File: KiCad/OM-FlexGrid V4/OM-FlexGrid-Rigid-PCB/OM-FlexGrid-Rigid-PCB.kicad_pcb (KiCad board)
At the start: 4 copper layers, 65.5 x 33 mm, 56 parts, among them IC1 ICM-42688-P, J1 Conn_01x06_Pin, J2 BAT Terminal, J3 Conn_01x20, J4 USB_C_Receptacle, J5 Conn_01x02, J6 Conn_01x03_Pin, J7 Conn_01x02_Pin, Q1 IRLML2060, Q2 VP0610T or BSS84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

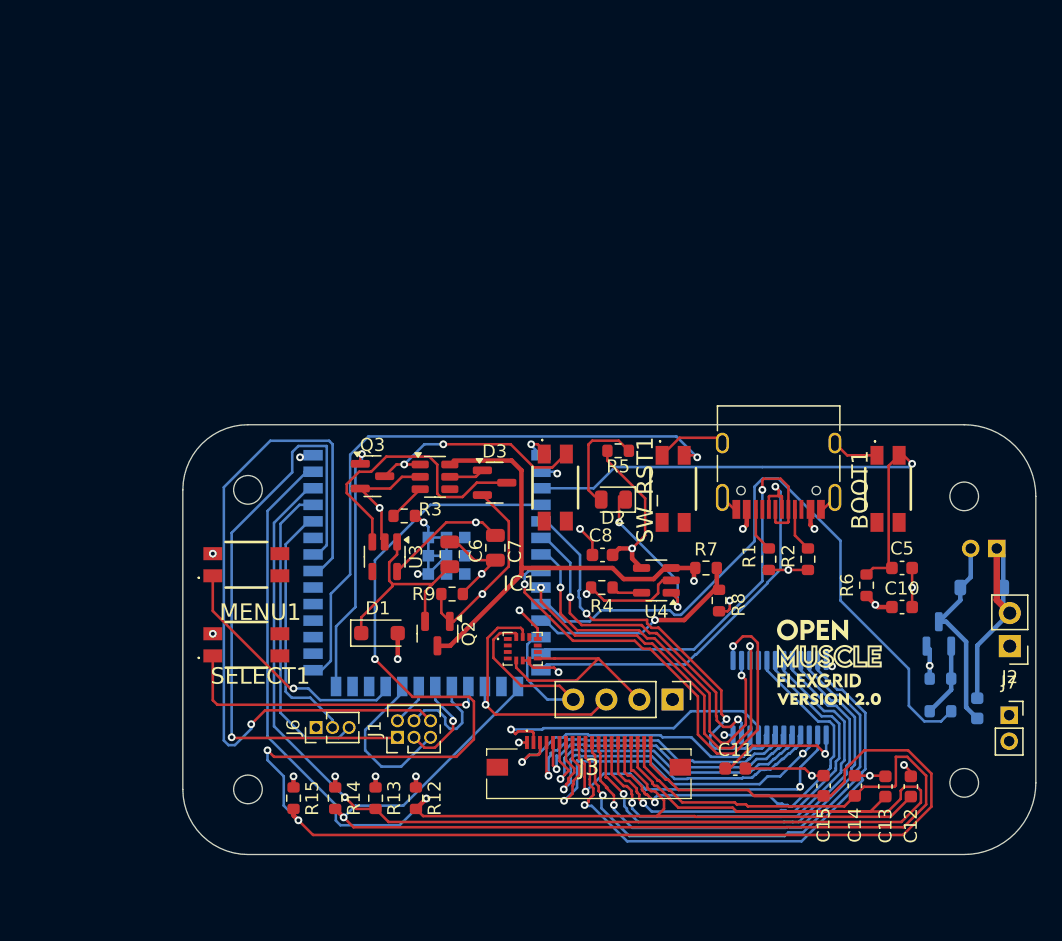
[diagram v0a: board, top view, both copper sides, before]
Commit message: V4 progress: SD card reader, RGB status LED, slimmer reoriented layout
What landed in V4 (Rigid PCB):
- microSD card socket added (data logging / model storage on-device)
- Discrete RGB status LED (5050 common-cathode driven by 3 PWM GPIOs,
  zero quiescent current vs WS2812 family; status palette ready to
  drive from firmware)
- Board orientation flipped for a slimmer profile that hugs the
  bracelet better; component placement reworked to clear the new
  long axis

Production artifacts included:
- V4 schematic (24K lines, full reroute from V3 baseline)
- V4 PCB with new placement
- V4 Gerber zip (OM-FlexGrid-Rigid-V4-Gerber.zip)
- JLCPCB plugin output dir (BOM + CPL ready for upload)
- Pick-and-place position file (.pos)
- 3D STEP export for mechanical fit check
- Per-revision backup snapshots from the design session

Housekeeping:
- .gitignore extended for KiCad transients (_autosave-*, *.lck,
  ~*.lck, tmp*.rpt) and .claude/ session metadata
- V3 working tree edits are intentionally left untouched; they
  belong to the V3 production-finalization branch of work

Status: V4 is "almost done" per the design pass; not yet ordered
or fab-validated. Treat this commit as a checkpoint, not a release.
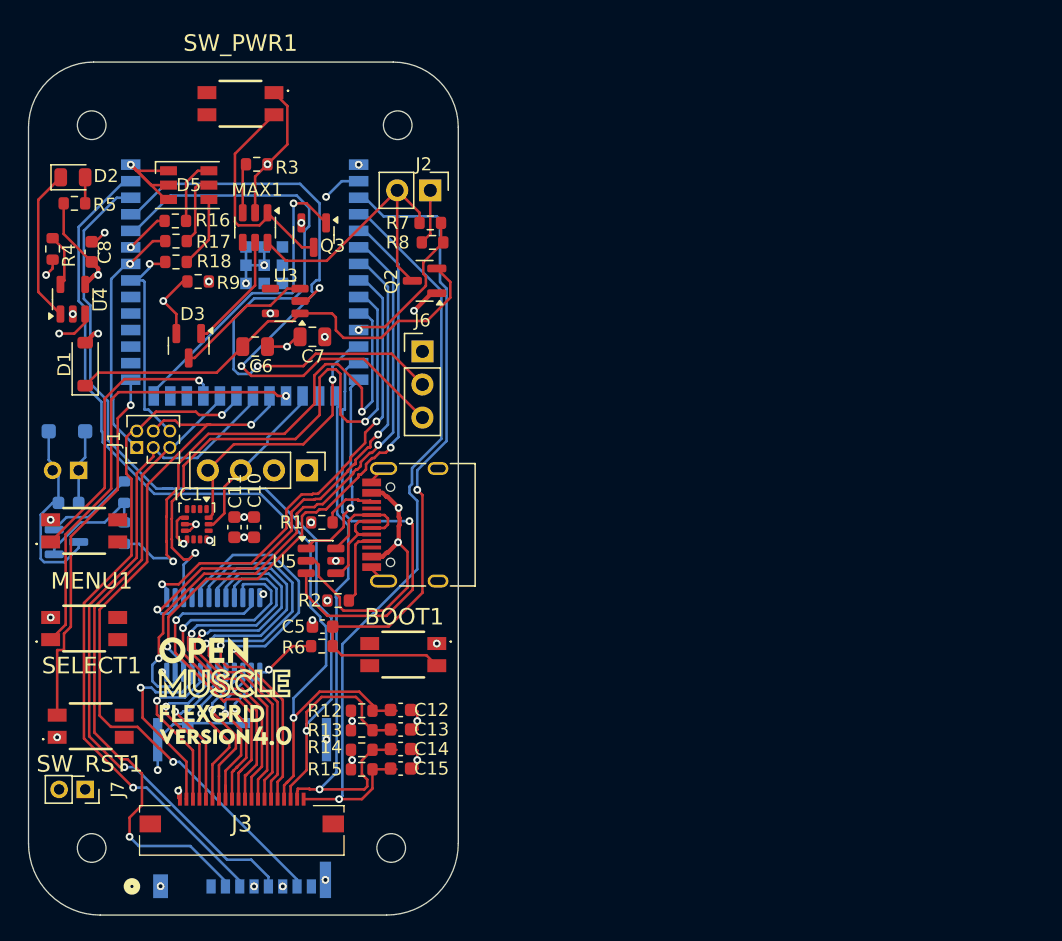
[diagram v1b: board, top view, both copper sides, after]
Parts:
- added D5: LED_RGB, LED_SMD:LED_RGB_PLCC-6, F.Cu at (152.4, 80.1)
- added J9: Micro_SD_Card, footprints:CONN_503398-1892_MOL, B.Cu at (156.6, 128.3)
- added R16: 330, Resistor_SMD:R_0603_1608Metric, F.Cu at (151.4, 82.8)
- added R17: 330, Resistor_SMD:R_0603_1608Metric, F.Cu at (151.5, 84.4)
- added R18: 330, Resistor_SMD:R_0603_1608Metric, F.Cu at (151.5, 86.0)
- added U5: USBLC6-2SC6, Package_TO_SOT_SMD:SOT-23-6, F.Cu at (162.6, 109.0)
- D1: footprint Diode_SMD:D_SOD-123F -> Diode_SMD:D_SOD-123
- D4: footprint Diode_SMD:D_SOD-123 -> Diode_SMD:D_SOD-123F
- IC1: footprint ICM-42688-P:IIM42352 -> Package_LGA:LGA-14_3x2.5mm_P0.5mm_LayoutBorder3x4y
- J6: footprint Connector_PinHeader_1.27mm:PinHeader_1x03_P1.27mm_Vertical -> Connector_PinHeader_2.54mm:PinHeader_1x03_P2.54mm_Vertical
- moved C9 71.5 mm to (143.2, 104.5), turned to 0 degrees
- moved D4 71.3 mm to (143.1, 99.0)
- moved J7 71.2 mm to (144.5, 126.5), turned to -90 degrees
- moved J5 70.8 mm to (144.0, 102.0)
- moved Q1 67.4 mm to (143.1, 107.5), turned to 0 degrees
- moved H3 67.2 mm to (145.0, 131.0), turned to -90 degrees
- moved R11 64.3 mm to (147.5, 103.7), turned to -90 degrees
- moved R10 64.1 mm to (147.5, 106.8), turned to -90 degrees
- moved J2 56.6 mm to (171.0, 80.5), turned to -90 degrees
- moved H4 52.4 mm to (145.0, 75.5), turned to -90 degrees
- moved H2 51.6 mm to (168.0, 131.0), turned to -90 degrees
- moved C10 50.1 mm to (157.5, 106.4), turned to 90 degrees
- moved U4 49.7 mm to (143.6, 88.9), turned to 90 degrees
- moved R4 49.5 mm to (142.0, 85.0), turned to -90 degrees
- moved D2 48.3 mm to (143.6, 79.5), turned to 0 degrees
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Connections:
- J4 pad A6: D+ -> Net-(J4-D+-PadA6)
- J4 pad A7: D- -> Net-(J4-D--PadA7)
- J4 pad B6: D+ -> Net-(J4-D+-PadA6)
- J4 pad B7: D- -> Net-(J4-D--PadA7)
- U2 pad 35: unconnected-(U2-IO42-Pad35) -> GP42
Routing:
- net ROW_3: track 142.8 -> 60.5 mm, vias 3 -> 1
- net ROW_2: track 94.9 -> 43.2 mm
- net SPI_MISO: track 8.23 -> 57.7 mm, vias 0 -> 2
- net SPI_MOSI: track 3.31 -> 52.0 mm, vias 0 -> 2
- net SPI_SCK: track 7.78 -> 53.4 mm
- net GP40: track 57.7 -> 17.0 mm
- net ROW_1: track 112.3 -> 74.3 mm
- net CS: track 12.5 -> 49.3 mm, vias 0 -> 1
- net RX: track 19.2 -> 48.8 mm, vias 0 -> 1
- net GP41: track 48.4 -> 19.2 mm
- net +3V3: track 41.1 -> 12.8 mm, vias 5 -> 8
- net TX: track 24.0 -> 48.0 mm, vias 0 -> 1
- net S1: track 26.4 -> 48.5 mm
- net VIN: track 16.4 -> 35.6 mm
- net 100: track 47.6 -> 28.4 mm
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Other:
- board size 65.5 x 33 mm -> 33 x 65.5 mm

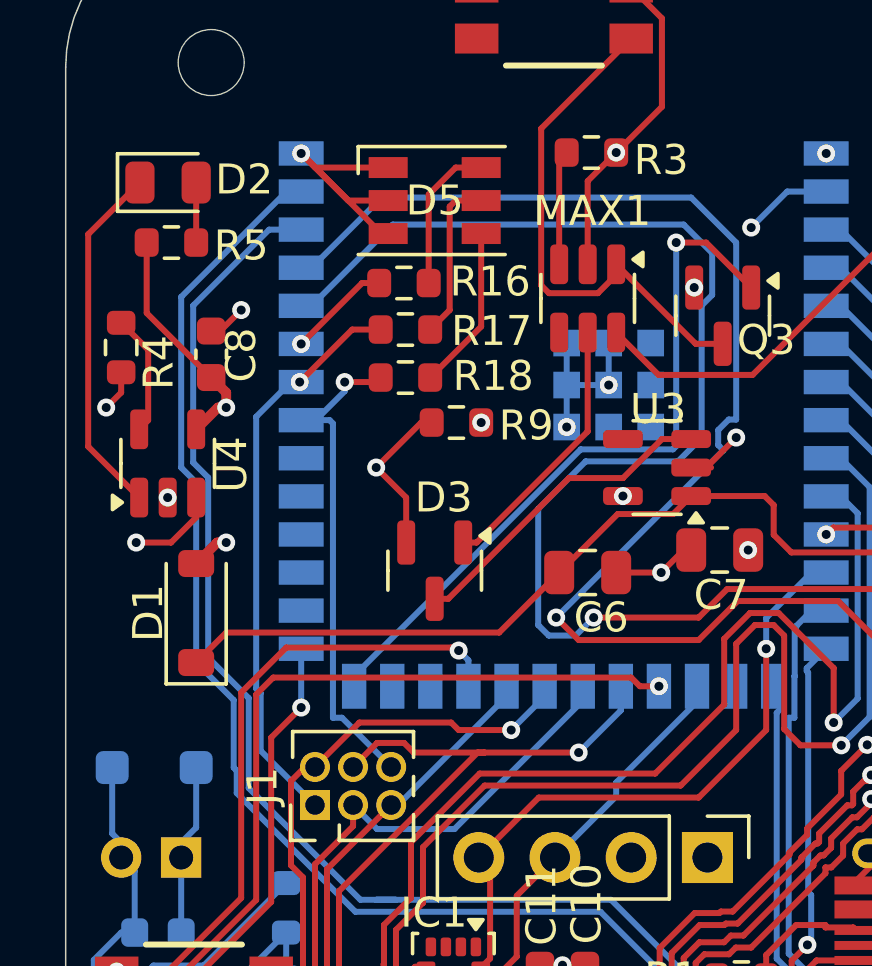
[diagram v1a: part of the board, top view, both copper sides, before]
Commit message: V4 rev: ADC matrix caps 2.2uF -> 100pF, MAX16054 footprint TSOT-23-6
Two real design changes applied to the V4 Rigid PCB this revision:

1. ADC matrix-row caps C12, C13, C14, C15 changed from 2.2 uF
   to 100 pF. This is Option 3 from the README's "Known carry-forward
   concerns" section. New LCSC: C14858 (100 pF 0603, Basic tier).
   RC time constant with the 10 kohm row pulldown drops from ~22 ms
   to ~1 us, well below the per-column ADC dwell time. Resolves the
   column-to-column bleed problem V3 saw with the 2.2 uF parts
   without sacrificing high-frequency noise filtering.

2. MAX1 (MAX16054 soft-power controller) footprint swapped from
   SOT-23-6 to TSOT-23-6. The LCSC part C79401 is actually
   MAX16054AZT+T which ships in TSOT-23-6. Pads are pad-compatible
   between SOT-23-6 and TSOT-23-6 (same pitch, same outline,
   thinner profile), so a part placed on the old footprint would
   have worked, but matching the schematic footprint to the actual
   package on disk is cleaner for downstream KiCad consumers.

3. Side change: MAX1's schematic value cleaned up from "~" to
   "MAX16054" so the BOM and silkscreen identify it properly.

Regenerated fab files in jlcpcb/ to reflect all three changes:
- gerber files updated
- BOM-OM-FlexGrid-Rigid-PCB.csv shows C12-C15 = 100 pF / C14858
- BOM also shows MAX1 / MAX16054 / TSOT-23-6
- CPL-OM-FlexGrid-Rigid-PCB.csv positions consistent

KiCad backups from the design session included in the commit.
V3 working-tree edits remain untouched.

Co-Authored-By: turfptax-claude O4.7 <turfptax-claude@openmuscle.org>
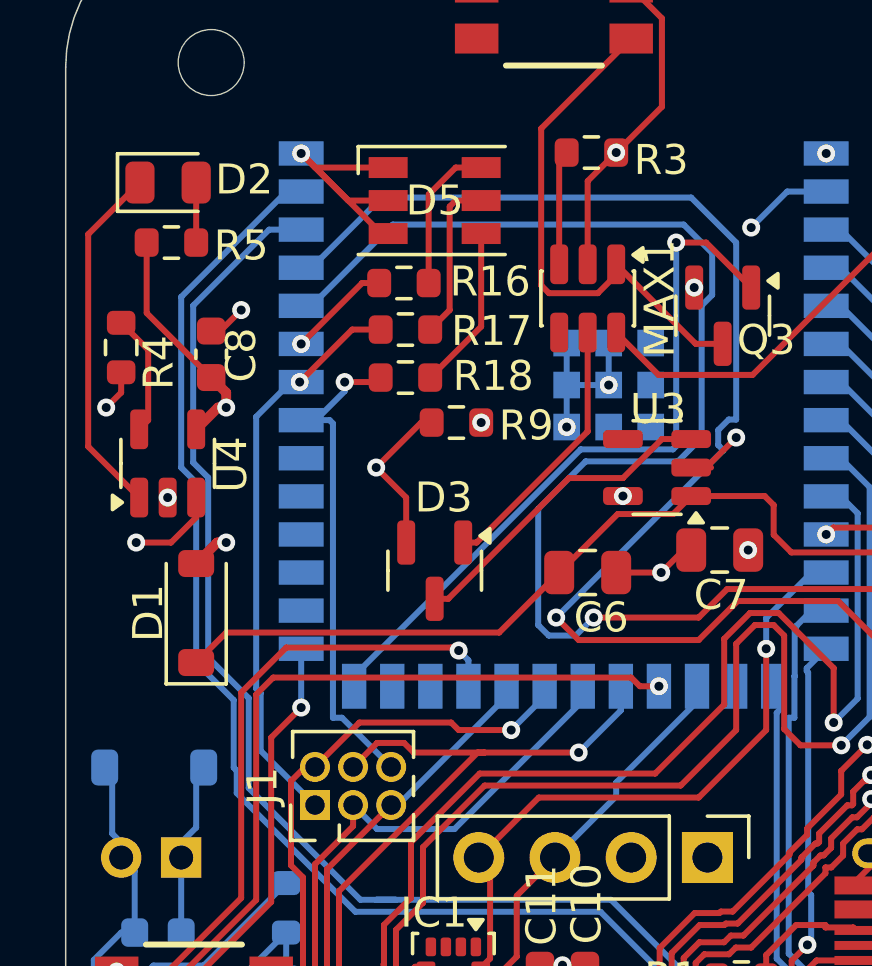
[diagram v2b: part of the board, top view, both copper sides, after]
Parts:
- C12, C13, C14, C15: value 2.2 uF -> 100 pF
- D4: footprint Diode_SMD:D_SOD-123F -> Diode_SMD:D_SOD-123
- MAX1: value ~ -> MAX16054; footprint Package_TO_SOT_SMD:SOT-23-6 -> Package_TO_SOT_SMD:TSOT-23-6
